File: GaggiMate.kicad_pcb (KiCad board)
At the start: 4 copper layers, 46 x 90 mm, 89 parts, among them J1 BTNS, J10 UART, J11 Fun breakout, J2 Heater SSR, J3 K-Type probe, J4 HX771, J5 Analog sensors, J6 Pressure Sensor, J7 LILYGO, J8 HV In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

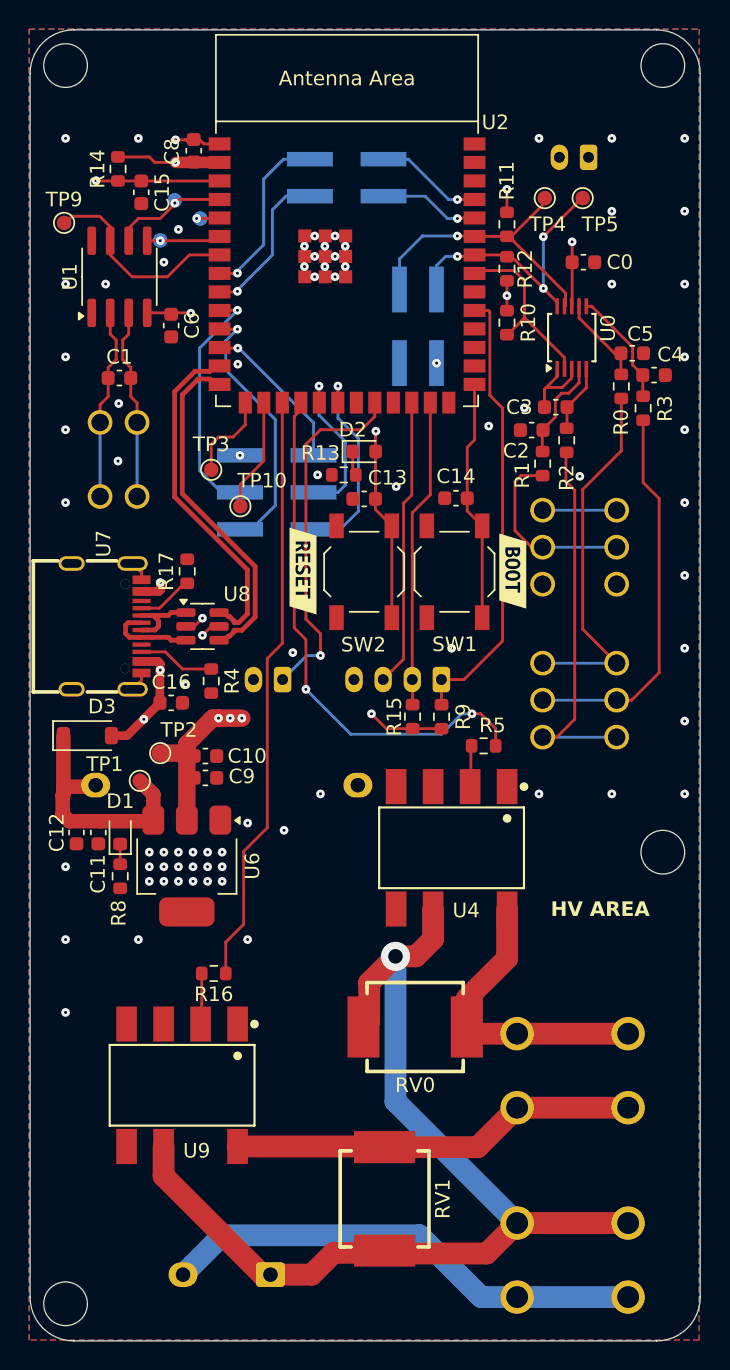
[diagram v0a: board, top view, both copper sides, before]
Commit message: update to new footprint ad make stuff nice
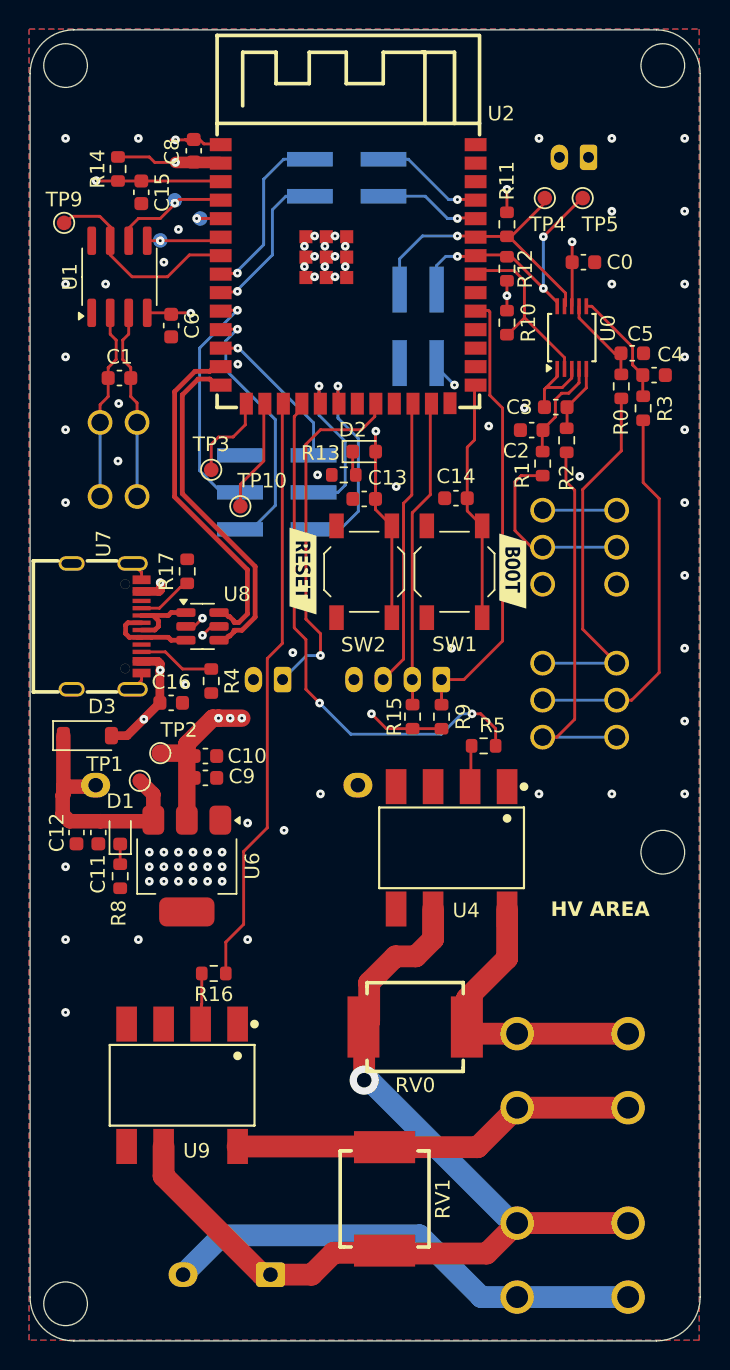
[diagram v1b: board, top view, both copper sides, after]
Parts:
- U2: footprint PCM_Espressif:ESP32-S3-WROOM-1 -> easyeda2kicad:WIRELM-SMD_ESP32-S3-WROOM-1
- moved U2 0.68 mm to (131.9, 66.8)
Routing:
- net HV_L: track 73.9 -> 70.4 mm
- net 3.3V: track 35.1 -> 37.2 mm
- net GND: vias 77 -> 76

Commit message: add missing models and finalize pcb
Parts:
- added D4: 3.3V LED, LED_SMD:LED_0603_1608Metric, F.Cu at (151.7, 61.5)
- added D5: 3.3V LED, LED_SMD:LED_0603_1608Metric, F.Cu at (153.3, 61.5)
- added R6: 150, Resistor_SMD:R_0603_1608Metric, F.Cu at (151.7, 64.5)
- added R7: 150, Resistor_SMD:R_0603_1608Metric, F.Cu at (153.3, 64.5)
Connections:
- U2 pad 38: unconnected-(U2-GPIO2/TOUCH2/ADC1_CH1-Pad38) -> LED2
- U2 pad 39: unconnected-(U2-GPIO1/TOUCH1/ADC1_CH0-Pad39) -> LED1
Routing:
- net LED2: track 0.00 -> 19.5 mm, vias 0 -> 2
- net LED1: track 0.00 -> 17.5 mm, vias 0 -> 2
- net Net-(D4-K): track 0.00 -> 1.40 mm
- net Net-(D5-K): track 0.00 -> 1.36 mm
- net GND: vias 76 -> 77
